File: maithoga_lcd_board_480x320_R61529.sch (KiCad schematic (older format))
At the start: 0 parts

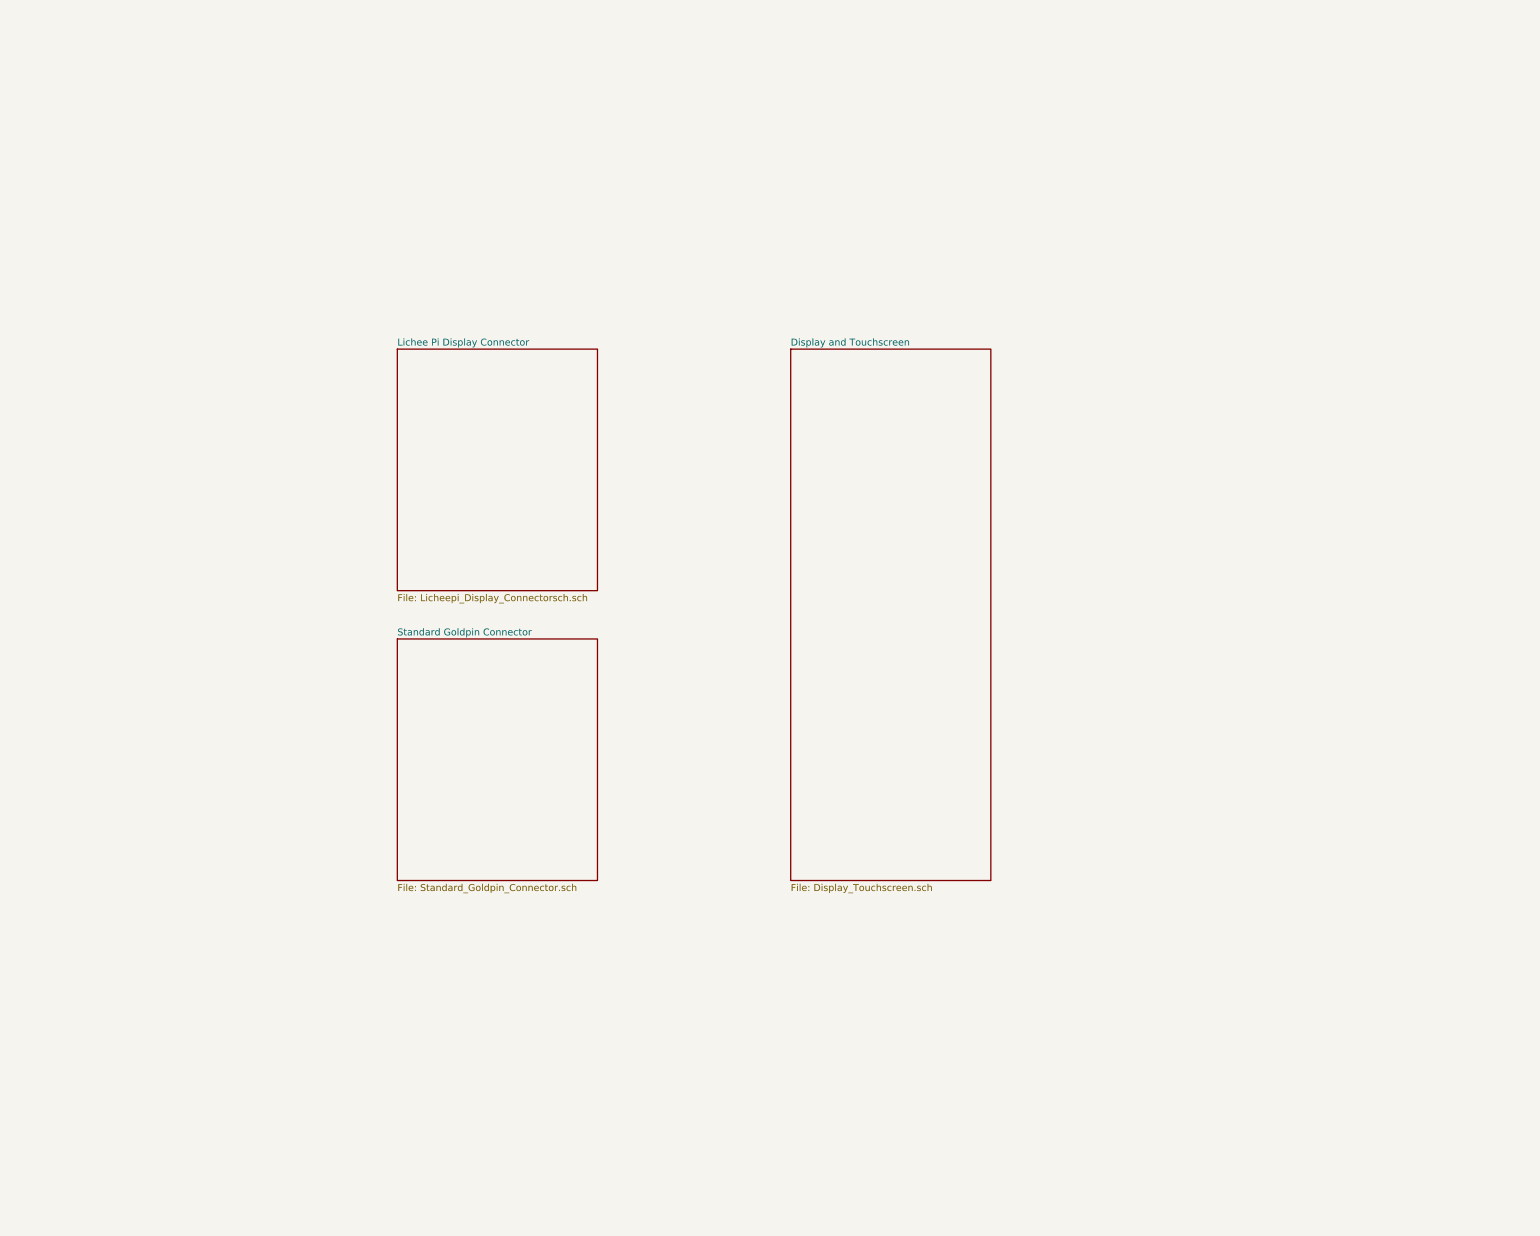
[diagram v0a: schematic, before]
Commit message: Filled hierarchical sheets
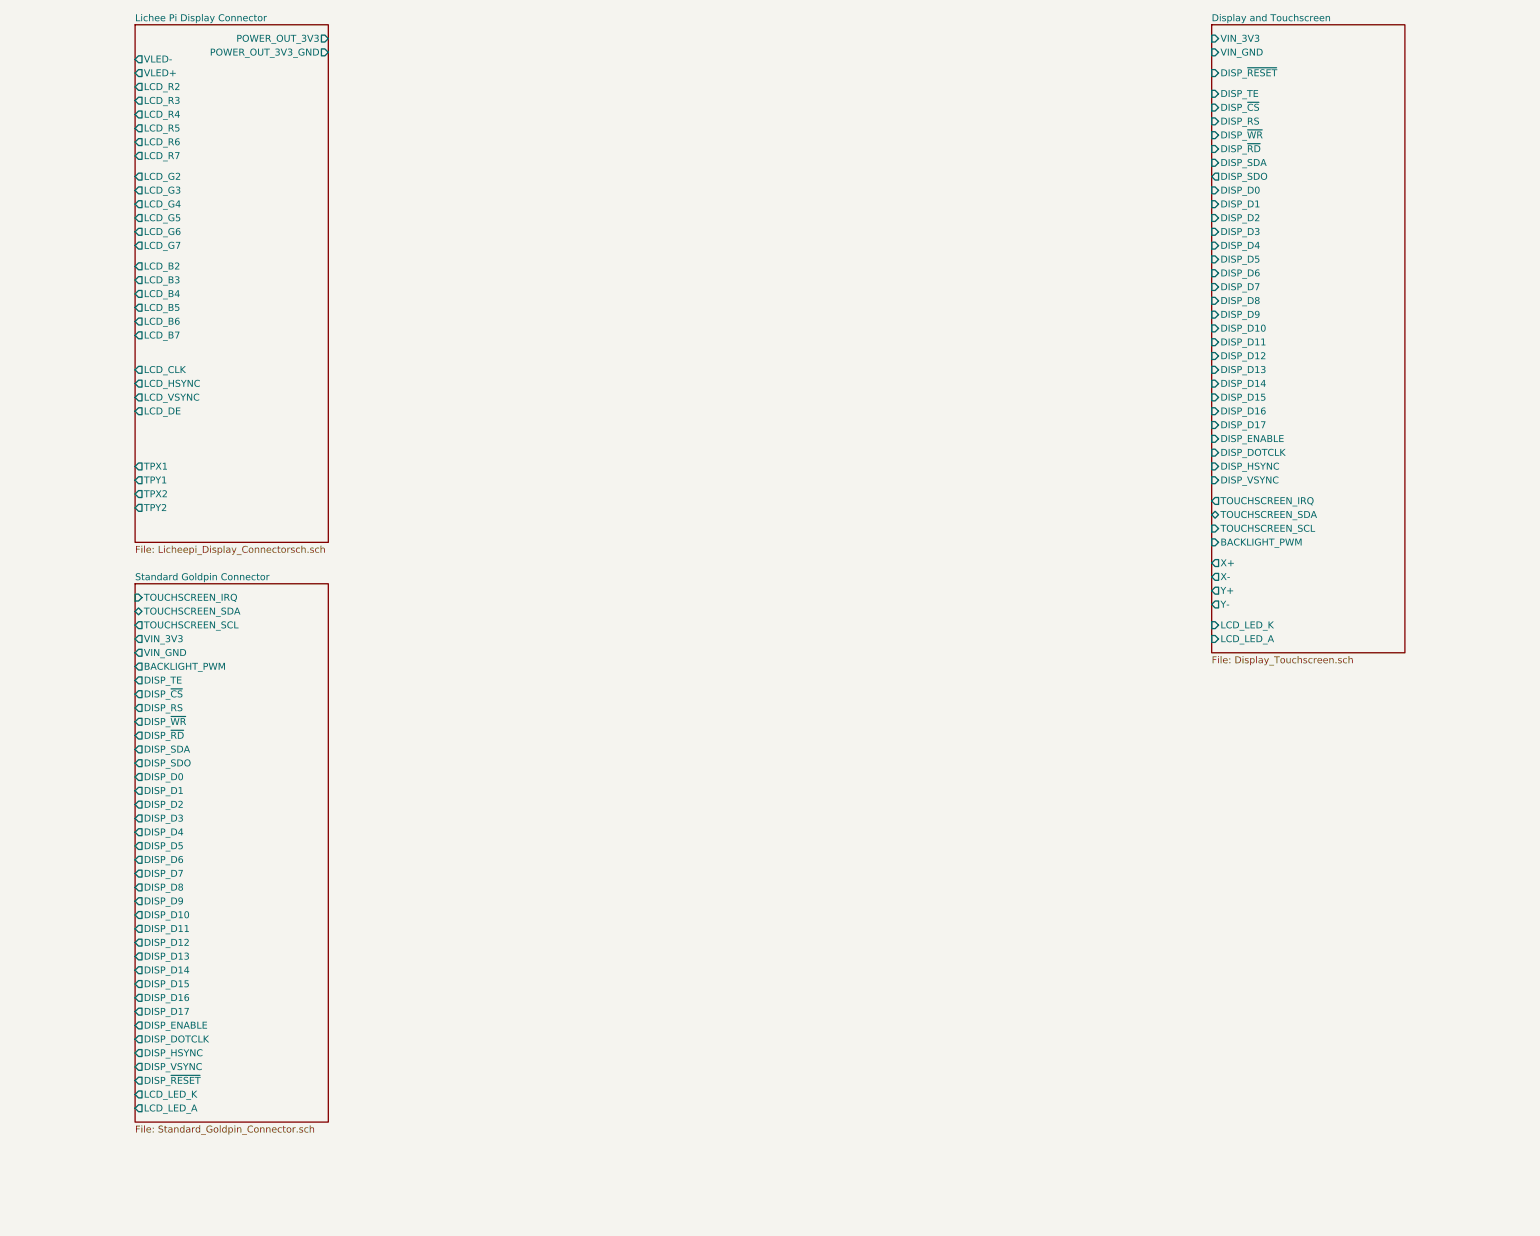
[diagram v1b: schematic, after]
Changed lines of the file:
@@
 $EndDescr
 $Sheet
-S 8700 3800 1450 3850
+S 11750 1450 1400 4550
 U 5F069040
 F0 "Display and Touchscreen" 50
 F1 "Display_Touchscreen.sch" 50
+F2 "TOUCHSCREEN_IRQ" O L 11750 4900 50
+F3 "TOUCHSCREEN_SDA" B L 11750 5000 50
+F4 "TOUCHSCREEN_SCL" I L 11750 5100 50
+F5 "VIN_3V3" I L 11750 1550 50
+F6 "VIN_GND" I L 11750 1650 50
+F7 "BACKLIGHT_PWM" I L 11750 5200 50
+F8 "DISP_TE" I L 11750 1950 50
+F9 "DISP_~CS~" I L 11750 2050 50
+F10 "DISP_RS" I L 11750 2150 50
+F11 "DISP_~WR~" I L 11750 2250 50
+F12 "DISP_~RD~" I L 11750 2350 50
+F13 "DISP_SDA" I L 11750 2450 50
+F14 "DISP_SDO" O L 11750 2550 50
+F15 "DISP_D0" I L 11750 2650 50
+F16 "DISP_D1" I L 11750 2750 50
+F17 "DISP_D2" I L 11750 2850 50
+F18 "DISP_D3" I L 11750 2950 50
+F19 "DISP_D4" I L 11750 3050 50
+F20 "DISP_D5" I L 11750 3150 50
+F21 "DISP_D6" I L 11750 3250 50
+F22 "DISP_D7" I L 11750 3350 50
+F23 "DISP_D8" I L 11750 3450 50
+F24 "DISP_D9" I L 11750 3550 50
+F25 "DISP_D10" I L 11750 3650 50
+F26 "DISP_D11" I L 11750 3750 50
+F27 "DISP_D12" I L 11750 3850 50
+F28 "DISP_D13" I L 11750 3950 50
+F29 "DISP_D14" I L 11750 4050 50
+F30 "DISP_D15" I L 11750 4150 50
+F31 "DISP_D16" I L 11750 4250 50
+F32 "DISP_D17" I L 11750 4350 50
+F33 "DISP_ENABLE" I L 11750 4450 50
+F34 "DISP_DOTCLK" I L 11750 4550 50
+F35 "DISP_HSYNC" I L 11750 4650 50
+F36 "DISP_VSYNC" I L 11750 4750 50
+F37 "DISP_~RESET~" I L 11750 1800 50
+F38 "X+" O L 11750 5350 50
+F39 "X-" O L 11750 5450 50
+F40 "Y+" O L 11750 5550 50
+F41 "Y-" O L 11750 5650 50
+F42 "LCD_LED_K" I L 11750 5800 50
+F43 "LCD_LED_A" I L 11750 5900 50
 $EndSheet
 $Sheet
-S 5850 3800 1450 1750
+S 3950 5500 1400 3900
+U 5F069099
+F0 "Standard Goldpin Connector" 50
+F1 "Standard_Goldpin_Connector.sch" 50
+F2 "TOUCHSCREEN_IRQ" I L 3950 5600 50
+F3 "TOUCHSCREEN_SDA" B L 3950 5700 50
+F4 "TOUCHSCREEN_SCL" O L 3950 5800 50
+F5 "VIN_3V3" O L 3950 5900 50
+F6 "VIN_GND" O L 3950 6000 50
+F7 "BACKLIGHT_PWM" O L 3950 6100 50
+F8 "DISP_TE" O L 3950 6200 50
+F9 "DISP_~CS~" O L 3950 6300 50
+F10 "DISP_RS" O L 3950 6400 50
+F11 "DISP_~WR~" O L 3950 6500 50
+F12 "DISP_~RD~" O L 3950 6600 50
+F13 "DISP_SDA" O L 3950 6700 50
+F14 "DISP_SDO" O L 3950 6800 50
+F15 "DISP_D0" O L 3950 6900 50
+F16 "DISP_D1" O L 3950 7000 50
+F17 "DISP_D2" O L 3950 7100 50
+F18 "DISP_D3" O L 3950 7200 50
+F19 "DISP_D4" O L 3950 7300 50
+F20 "DISP_D5" O L 3950 7400 50
+F21 "DISP_D6" O L 3950 7500 50
+F22 "DISP_D7" O L 3950 7600 50
+F23 "DISP_D8" O L 3950 7700 50
+F24 "DISP_D9" O L 3950 7800 50
+F25 "DISP_D10" O L 3950 7900 50
+F26 "DISP_D11" O L 3950 8000 50
+F27 "DISP_D12" O L 3950 8100 50
+F28 "DISP_D13" O L 3950 8200 50
+F29 "DISP_D14" O L 3950 8300 50
+F30 "DISP_D15" O L 3950 8400 50
+F31 "DISP_D16" O L 3950 8500 50
+F32 "DISP_D17" O L 3950 8600 50
+F33 "DISP_ENABLE" O L 3950 8700 50
+F34 "DISP_DOTCLK" O L 3950 8800 50
+F35 "DISP_HSYNC" O L 3950 8900 50
+F36 "DISP_VSYNC" O L 3950 9000 50
+F37 "DISP_~RESET~" O L 3950 9100 50
+F38 "LCD_LED_K" O L 3950 9200 50
+F39 "LCD_LED_A" O L 3950 9300 50
+$EndSheet
+$Sheet
+S 3950 1450 1400 3750
 U 5F06906E
 F0 "Lichee Pi Display Connector" 50
 F1 "Licheepi_Display_Connectorsch.sch" 50
-$EndSheet
-$Sheet
-S 5850 5900 1450 1750
-U 5F069099
-F0 "Standard Goldpin Connector" 50
-F1 "Standard_Goldpin_Connector.sch" 50
+F2 "VLED-" O L 3950 1700 50
+F3 "VLED+" O L 3950 1800 50
+F4 "LCD_R2" O L 3950 1900 50
+F5 "LCD_R3" O L 3950 2000 50
+F6 "LCD_R4" O L 3950 2100 50
+F7 "LCD_R5" O L 3950 2200 50
+F8 "LCD_R6" O L 3950 2300 50
+F9 "LCD_R7" O L 3950 2400 50
+F10 "LCD_G2" O L 3950 2550 50
+F11 "LCD_G3" O L 3950 2650 50
+F12 "LCD_G4" O L 3950 2750 50
+F13 "LCD_G5" O L 3950 2850 50
+F14 "LCD_G6" O L 3950 2950 50
+F15 "LCD_G7" O L 3950 3050 50
+F16 "LCD_B2" O L 3950 3200 50
+F17 "LCD_B3" O L 3950 3300 50
+F18 "LCD_B4" O L 3950 3400 50
+F19 "LCD_B5" O L 3950 3500 50
+F20 "LCD_B6" O L 3950 3600 50
+F21 "LCD_B7" O L 3950 3700 50
+F22 "LCD_CLK" O L 3950 3950 50
+F23 "LCD_HSYNC" O L 3950 4050 50
+F24 "LCD_VSYNC" O L 3950 4150 50
+F25 "LCD_DE" O L 3950 4250 50
+F26 "TPX1" O L 3950 4650 50
+F27 "TPY1" O L 3950 4750 50
+F28 "TPX2" O L 3950 4850 50
+F29 "TPY2" O L 3950 4950 50
+F30 "POWER_OUT_3V3" O R 5350 1550 50
+F31 "POWER_OUT_3V3_GND" O R 5350 1650 50
 $EndSheet
 $EndSCHEMATC

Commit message: Schematic ready, need check
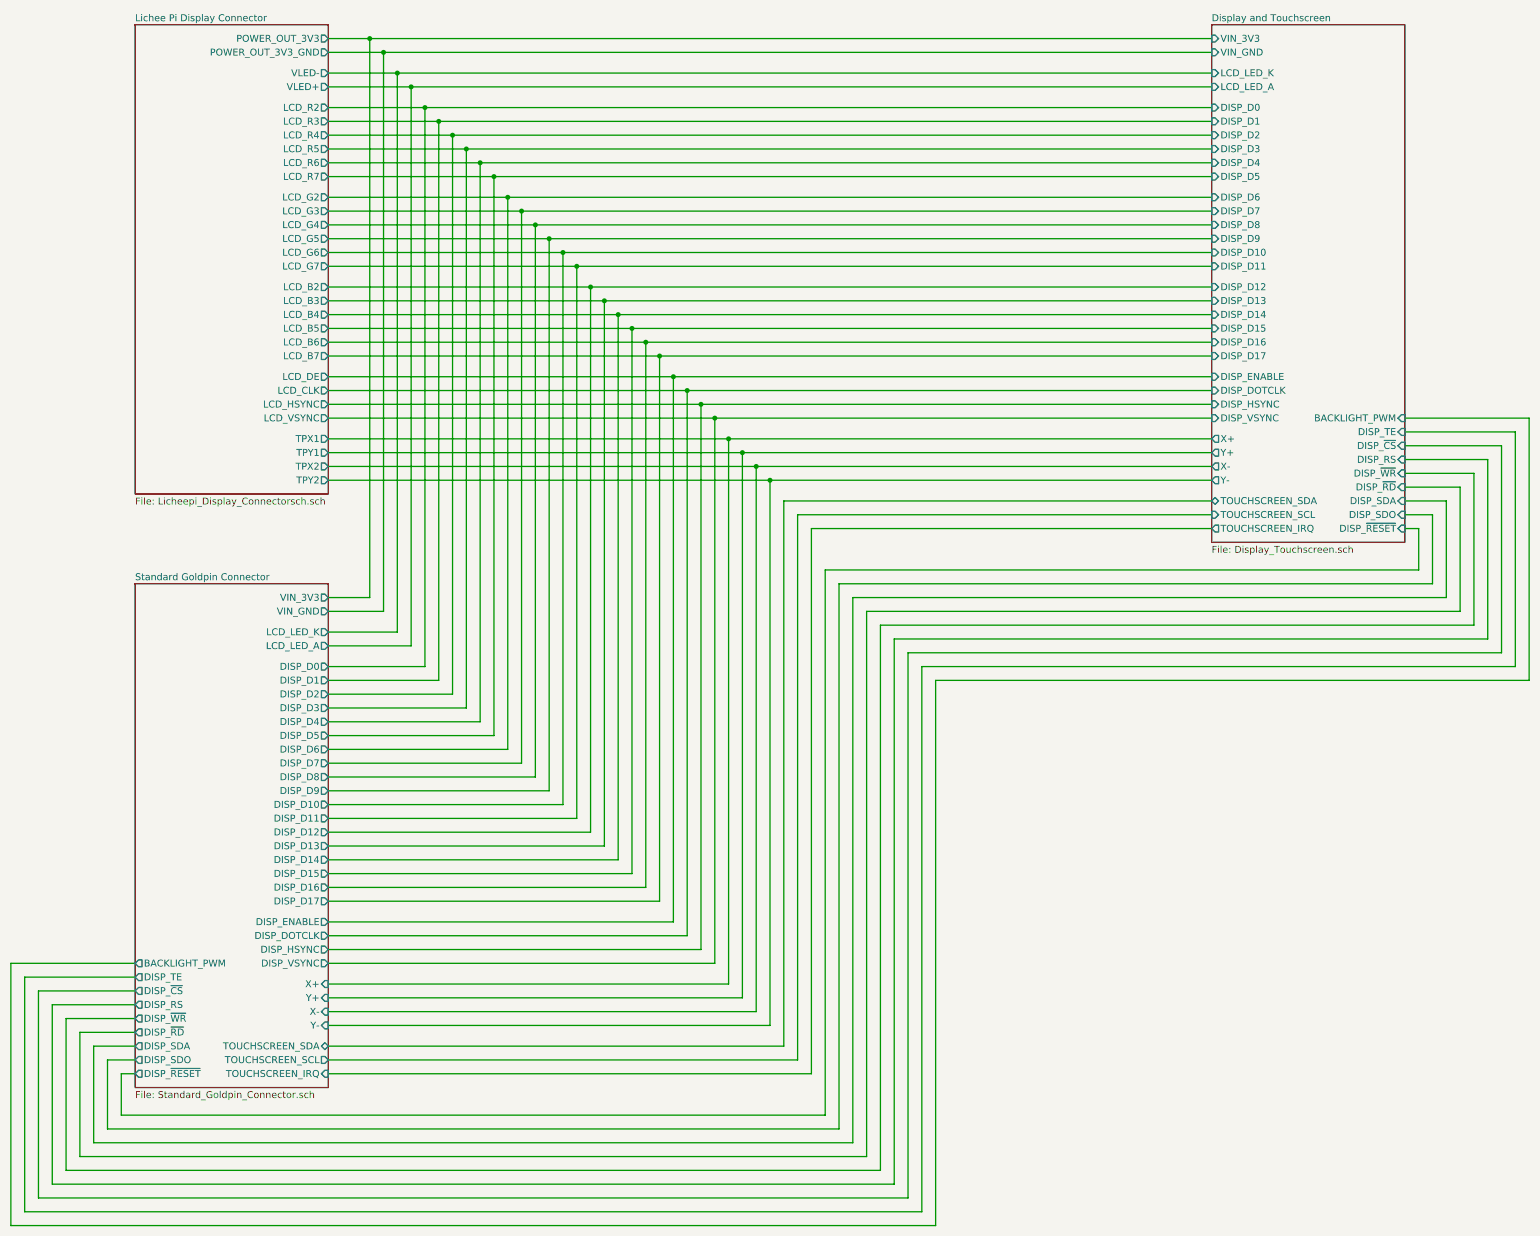
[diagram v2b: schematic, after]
